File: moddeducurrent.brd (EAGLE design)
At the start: 50.6 x 46.5 mm, 29 parts, among them IC1 TLC251D, IC2 LMV321M5X, X1 USBPCB, X2 USBOLD

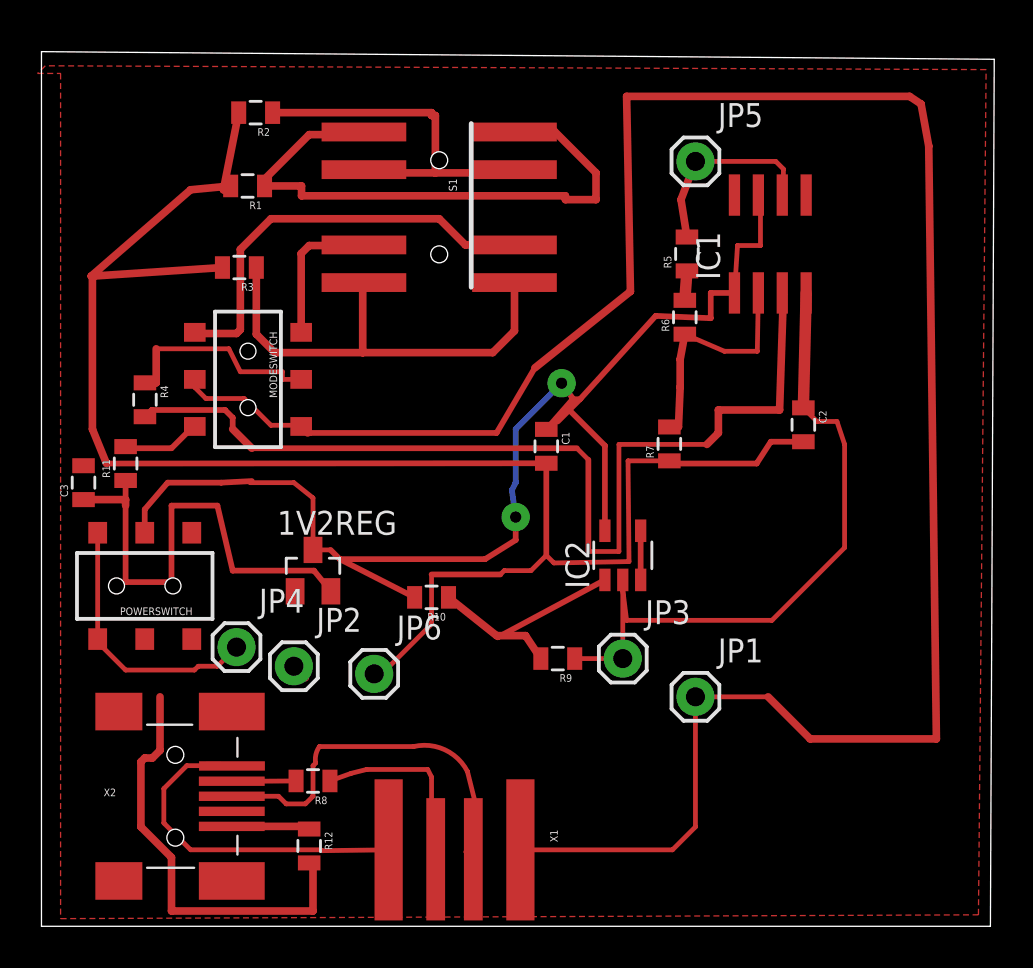
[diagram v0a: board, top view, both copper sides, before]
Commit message: current traces no longer shared with voltage traces.
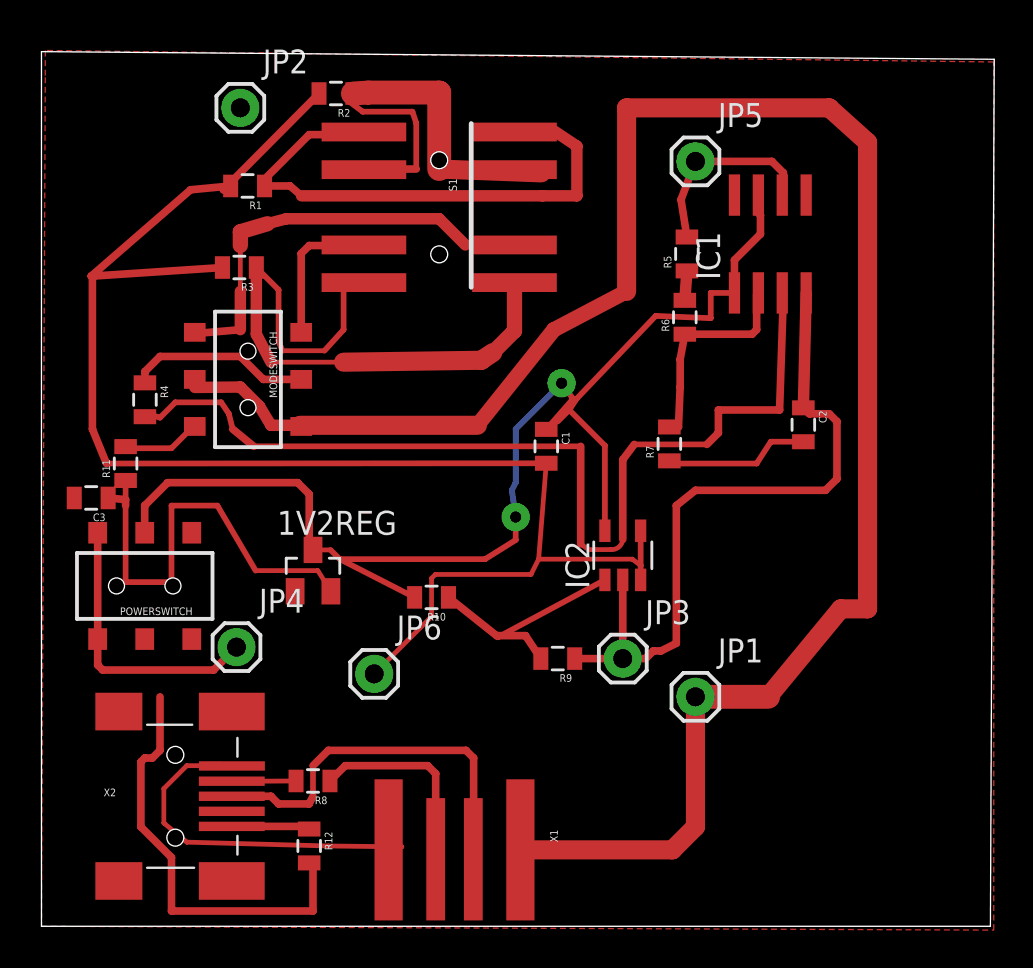
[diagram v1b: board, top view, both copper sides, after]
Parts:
- moved JP2 29.8 mm to (9.75, 78.0)
- moved R2 4.39 mm to (14.8, 78.8)
- moved C3 0.91 mm to (1.83, 57.3), turned to 180 degrees
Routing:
- net PROBE: track 118.3 -> 103.5 mm
- net CSR3: track 24.5 -> 33.6 mm
- net CSR2: track 20.3 -> 25.1 mm
- net GND: track 118.9 -> 114.2 mm
- net CSR1: track 31.7 -> 29.7 mm
- net N$4: track 26.2 -> 24.2 mm
- net AMPIN: track 11.3 -> 9.74 mm
- net N$9: track 12.6 -> 11.3 mm
- net VUSB_EXTERN: track 18.5 -> 19.7 mm
- net V+: track 70.1 -> 69.3 mm
- net VBAT: track 14.3 -> 15.0 mm

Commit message: Added missing input capacitor on 1V2REG just in case, fixed a piee of atrocious routing on the output cap of the same, beefed up the main current carrying trace.
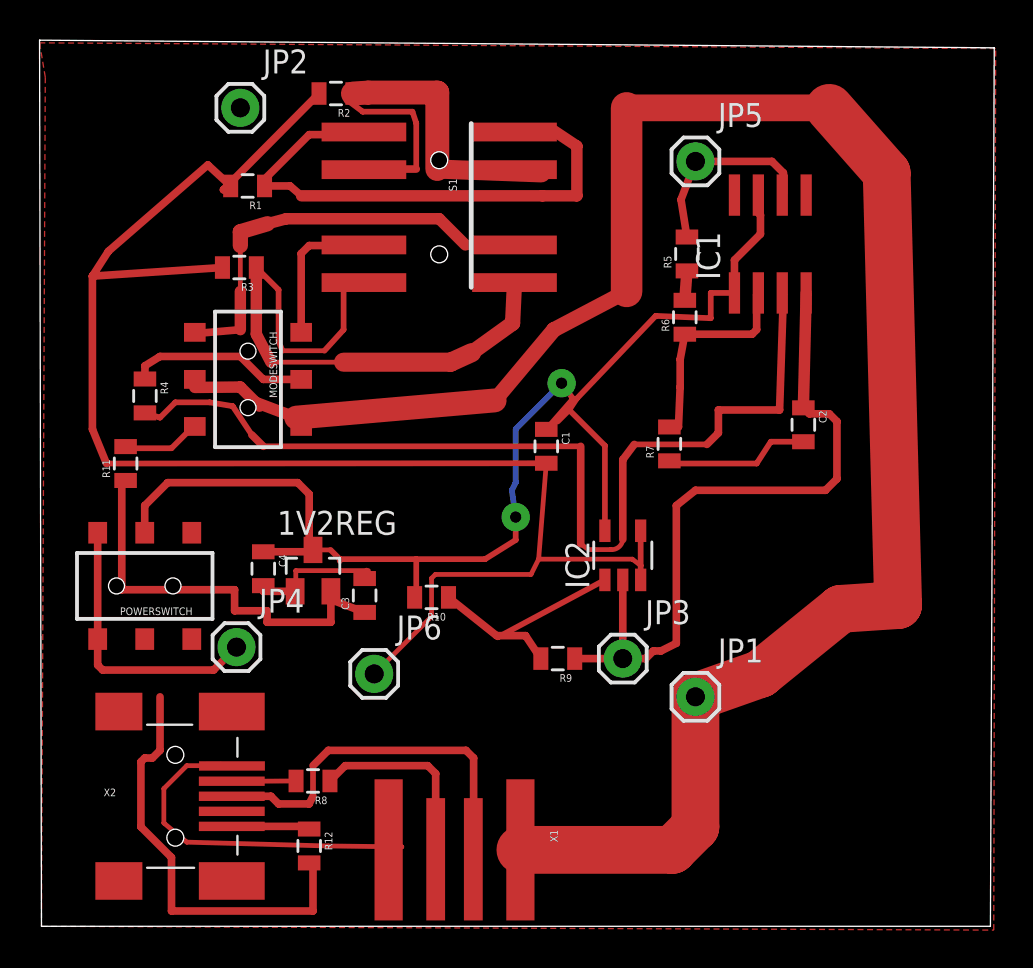
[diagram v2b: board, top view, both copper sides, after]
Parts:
- added C4: (no value), SparkFun - Copy:0805
- moved C3 15.4 mm to (16.4, 52.1), turned to 90 degrees
- moved R4 0.20 mm to (4.69, 62.7)
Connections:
- net GND: now also C4.2
- net V+: now also C4.1
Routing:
- net GND: track 114.2 -> 122.7 mm
- net N$4: track 24.2 -> 22.8 mm
- net CSR2: track 25.1 -> 25.7 mm
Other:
- board size 50.6 x 46.5 mm -> 50.7 x 47.1 mm

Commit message: Changed switch to cheaper ebay switch. Added signal plane.
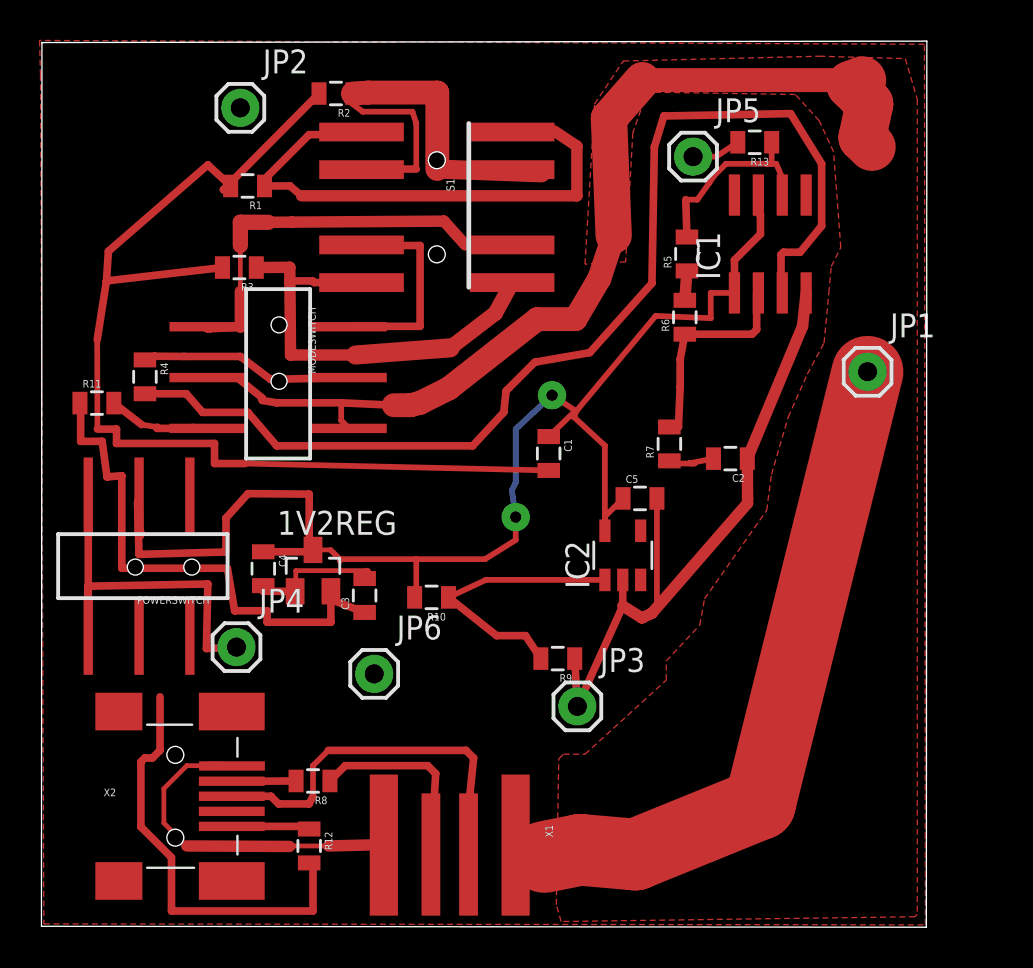
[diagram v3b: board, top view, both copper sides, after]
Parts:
- added C5, R13: (no value), SparkFun - Copy:0805
- MODESWITCH: value AYZ0202 -> SWITCH-DPDTDPDTSMDBENT; device SparkFun - Copy:AYZ0202 -> ebay:AYZ0202
- POWERSWITCH: value SWITCH-DPDTSMD -> SWITCH-DPDTDPDTSMDBENT; device SparkFun - Copy:AYZ0202 -> ebay:AYZ0202
- moved JP1 19.5 mm to (43.1, 64.0)
- moved C2 4.28 mm to (35.8, 59.4), turned to 180 degrees
- moved R11 3.56 mm to (2.13, 62.3), turned to 0 degrees
- moved JP3 3.50 mm to (27.7, 46.2)
- moved MODESWITCH 2.16 mm to (11.8, 65.0)
- moved POWERSWITCH 1.41 mm to (5.67, 53.6)
- moved R4 1.02 mm to (4.69, 63.7)
- moved C1 0.40 mm to (26.1, 59.7)
- moved X1 0.36 mm to (20.9, 38.7)
- moved JP5 0.28 mm to (33.8, 75.4)
- moved S1 0.13 mm to (20.2, 72.7)
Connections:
- new net N$2: JP5.1, R13.2
- net OUT: now also R13.1; no longer JP5.1
- net V+: now also C5.1
- net V-: now also C5.2
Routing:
- net GND: track 122.7 -> 91.5 mm
- net PROBE: track 104.0 -> 90.8 mm
- net CSR3: track 33.1 -> 23.7 mm
- net VBAT: track 15.0 -> 21.7 mm
- net N$7: track 53.0 -> 59.4 mm
- net V+: track 69.8 -> 75.7 mm
- net N$4: track 22.8 -> 28.4 mm
- net CSOUT: track 7.71 -> 11.2 mm
- net CCSOURCE: track 4.19 -> 7.37 mm
- net N$2: track 0.00 -> 2.61 mm
- net AMPIN: track 9.65 -> 11.3 mm
- net VUSB_EXTERN: track 19.7 -> 18.2 mm
- net N$17: track 16.1 -> 14.8 mm
- net OUT: track 10.3 -> 10.9 mm
- added copper zone on layer 1, net PROBE
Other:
- board size 50.7 x 47.1 mm -> 47 x 47.1 mm

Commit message: added resistor values
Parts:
- C1, C2, C3, C4, C5: value (none) -> 0.1u
- R1: value (none) -> 10k 0.1%
- R10, R9: value (none) -> 100k 1%
- R11: value 120ohm -> 120ohm 0.1%
- R12: value (none) -> 0R
- R13: value (none) -> 100R
- R2: value (none) -> 10R 0.1%
- R3: value (none) -> 0R01 0.1%
- R4: value (none) -> 100R 1%
- R5: value (none) -> 75k 0.1%
- R6: value (none) -> 24k 0.1%
- R7: value (none) -> 1k 0.1%
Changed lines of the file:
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@@
 <elements>
 <element name="IC1" library="linear" package="SO08" value="TLC251D" x="37.9116" y="70.7952"/>
-<element name="C1" library="SparkFun - Copy" package="0805" value="" x="26.1366" y="59.6646" rot="R270"/>
-<element name="C2" library="SparkFun - Copy" package="0805" value="" x="35.79" y="59.3916" rot="R180"/>
-<element name="R1" library="SparkFun - Copy" package="0805" value="" x="10.1396" y="73.8796" rot="R180"/>
-<element name="R2" library="SparkFun - Copy" package="0805" value="" x="14.8336" y="78.7908" rot="R180"/>
-<element name="R3" library="SparkFun - Copy" package="0805" value="" x="9.7028" y="69.5452" rot="R180"/>
-<element name="R4" library="SparkFun - Copy" package="0805" value="" x="4.6852" y="63.7384" rot="R270"/>
-<element name="R5" library="SparkFun - Copy" package="0805" value="" x="33.4824" y="70.2664" rot="R90"/>
-<element name="R6" library="SparkFun - Copy" package="0805" value="" x="33.3696" y="66.9024" rot="R90"/>
-<element name="R7" library="SparkFun - Copy" package="0805" value="" x="32.5488" y="60.174" rot="R90"/>
+<element name="C1" library="SparkFun - Copy" package="0805" value="0.1u" x="26.1366" y="59.6646" rot="R270"/>
+<element name="C2" library="SparkFun - Copy" package="0805" value="0.1u" x="35.79" y="59.3916" rot="R180"/>
+<element name="R1" library="SparkFun - Copy" package="0805" value="10k 0.1%" x="10.1396" y="73.8796" rot="R180"/>
+<element name="R2" library="SparkFun - Copy" package="0805" value="10R 0.1%" x="14.8336" y="78.7908" rot="R180"/>
+<element name="R3" library="SparkFun - Copy" package="0805" value="0R01 0.1%" x="9.7028" y="69.5452" rot="R180"/>
+<element name="R4" library="SparkFun - Copy" package="0805" value="100R 1%" x="4.6852" y="63.7384" rot="R270"/>
+<element name="R5" library="SparkFun - Copy" package="0805" value="75k 0.1%" x="33.4824" y="70.2664" rot="R90"/>
+<element name="R6" library="SparkFun - Copy" package="0805" value="24k 0.1%" x="33.3696" y="66.9024" rot="R90"/>
+<element name="R7" library="SparkFun - Copy" package="0805" value="1k 0.1%" x="32.5488" y="60.174" rot="R90"/>
 <element name="X1" library="SparkFun - Copy" package="USB-A-PCB" value="USBPCB" x="20.8788" y="38.6588" rot="R270"/>
 <element name="X2" library="SparkFun - Copy" package="USB-MINIB-OLD" value="USBOLD" x="6.2992" y="41.4528"/>
 <element name="IC2" library="linear" package="SOT23-5" value="LMV321M5X" x="30.0736" y="54.2544"/>
 <element name="POWERSWITCH" library="ebay" package="AYZ0202" value="SWITCH-DPDTDPDTSMDBENT" x="5.6736" y="53.6288" rot="R180"/>
-<element name="R9" library="SparkFun - Copy" package="0805" value="" x="26.6192" y="48.768" rot="R180"/>
-<element name="R10" library="SparkFun - Copy" package="0805" value="" x="19.9136" y="52.0192" rot="R180"/>
+<element name="R9" library="SparkFun - Copy" package="0805" value="100k 1%" x="26.6192" y="48.768" rot="R180"/>
+<element name="R10" library="SparkFun - Copy" package="0805" value="100k 1%" x="19.9136" y="52.0192" rot="R180"/>
 <element name="1V2REG" library="linear" package="SOT23" value="MCP1703CB" x="13.6144" y="53.4416"/>
-<element name="C3" library="SparkFun - Copy" package="0805" value="" x="16.3576" y="52.1208" rot="R90"/>
+<element name="C3" library="SparkFun - Copy" package="0805" value="0.1u" x="16.3576" y="52.1208" rot="R90"/>
 <element name="MODESWITCH" library="ebay" package="AYZ0202" value="SWITCH-DPDTDPDTSMDBENT" x="11.811" y="64.9986" rot="R270"/>
-<element name="R11" library="SparkFun - Copy" package="0805" value="120ohm" x="2.1312" y="62.3424"/>
+<element name="R11" library="SparkFun - Copy" package="0805" value="120ohm 0.1%" x="2.1312" y="62.3424"/>
 <element name="JP1" library="SparkFun - Copy" package="1X01" value="M01PTH" x="43.0784" y="64.008"/>
 <element name="JP3" library="SparkFun - Copy" package="1X01" value="M01PTH" x="27.6606" y="46.228"/>
@@
 <element name="JP2" library="SparkFun - Copy" package="1X01" value="M01PTH" x="9.7536" y="78.0288"/>
 <element name="R8" library="SparkFun - Copy" package="0805" value="0ohm" x="13.6144" y="42.2656" rot="R180"/>
-<element name="R12" library="SparkFun - Copy" package="0805" value="" x="13.4112" y="38.8112" rot="R270"/>
+<element name="R12" library="SparkFun - Copy" package="0805" value="0R" x="13.4112" y="38.8112" rot="R270"/>
 <element name="S1" library="LL" package="SWITCH-DP3T-SMD" value="" x="20.193" y="72.7456" rot="R270"/>
-<element name="C4" library="SparkFun - Copy" package="0805" value="" x="10.9728" y="53.5432" rot="R270"/>
-<element name="R13" library="SparkFun - Copy" package="0805" value="" x="37.084" y="76.2" rot="R180"/>
-<element name="C5" library="SparkFun - Copy" package="0805" value="" x="30.988" y="57.277"/>
+<element name="C4" library="SparkFun - Copy" package="0805" value="0.1u" x="10.9728" y="53.5432" rot="R270"/>
+<element name="R13" library="SparkFun - Copy" package="0805" value="100R" x="37.084" y="76.2" rot="R180"/>
+<element name="C5" library="SparkFun - Copy" package="0805" value="0.1u" x="30.988" y="57.277"/>
 </elements>
 <signals>
@@
 </signal>
 </signals>
-<errors>
-</errors>
 </board>
 </drawing>
